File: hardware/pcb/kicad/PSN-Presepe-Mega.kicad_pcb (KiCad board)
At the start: 2 copper layers, 280 x 170 mm, 83 parts, among them J1 12V_IN, K1 G5Q-1_DC12, K10 G5Q-1_DC12, K11 G5Q-1_DC12, K12 G5Q-1_DC12, K13 G5Q-1_DC12, K14 G5Q-1_DC12, K15 G5Q-1_DC12, K16 G5Q-1_DC12, K2 G5Q-1_DC12, K3 G5Q-1_DC12, K4 G5Q-1_DC12, K5 G5Q-1_DC12, K6 G5Q-1_DC12, K7 G5Q-1_DC12, K8 G5Q-1_DC12, K9 G5Q-1_DC12, Q1 IRLZ44N_CIELO_R, Q2 IRLZ44N_CIELO_G, Q3 IRLZ44N_CIELO_B, Q4 IRLZ44N_TRAM_R, Q5 IRLZ44N_TRAM_G, Q6 IRLZ44N_TRAM_B, Q7 IRLZ44N_ALBA_R, Q8 IRLZ44N_ALBA_G, Q9 IRLZ44N_ALBA_B, U1 ULN2803C, U2 ULN2803C

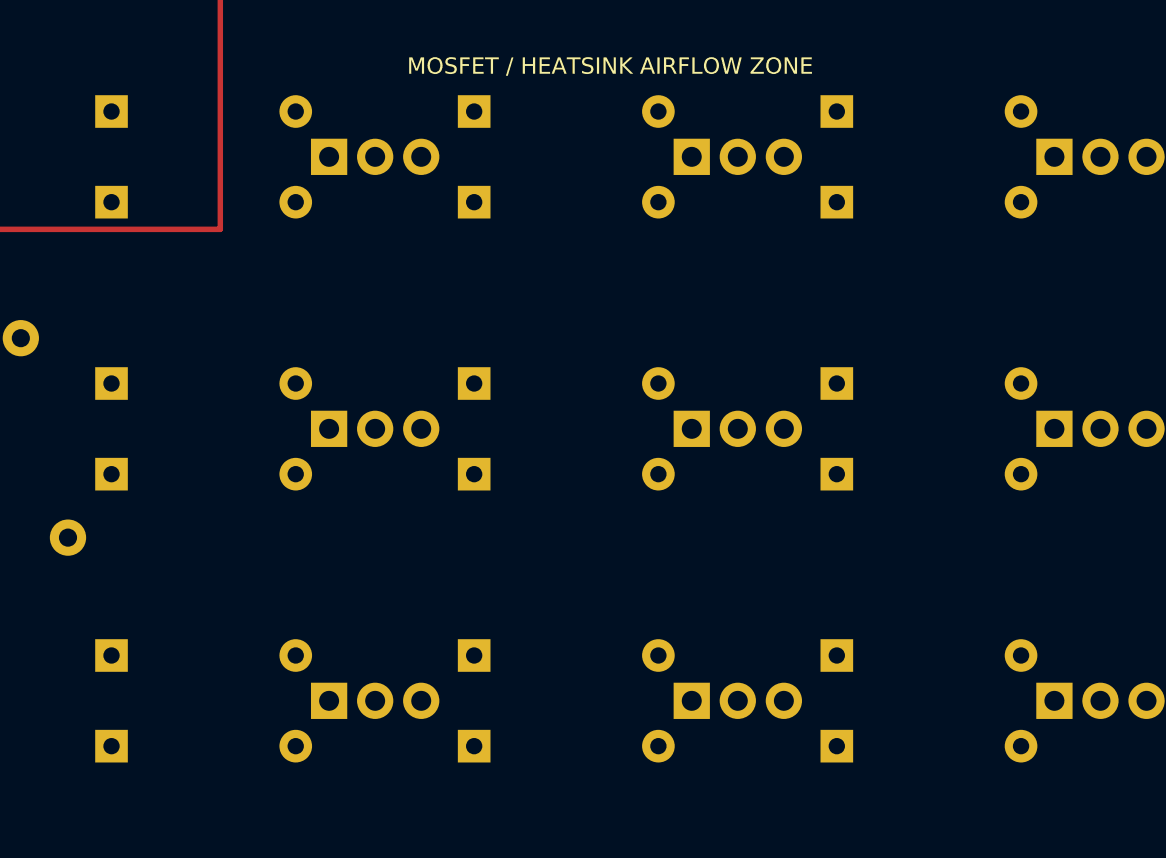
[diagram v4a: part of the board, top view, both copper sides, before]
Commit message: Promote DRC-clean local MOSFET gate routing
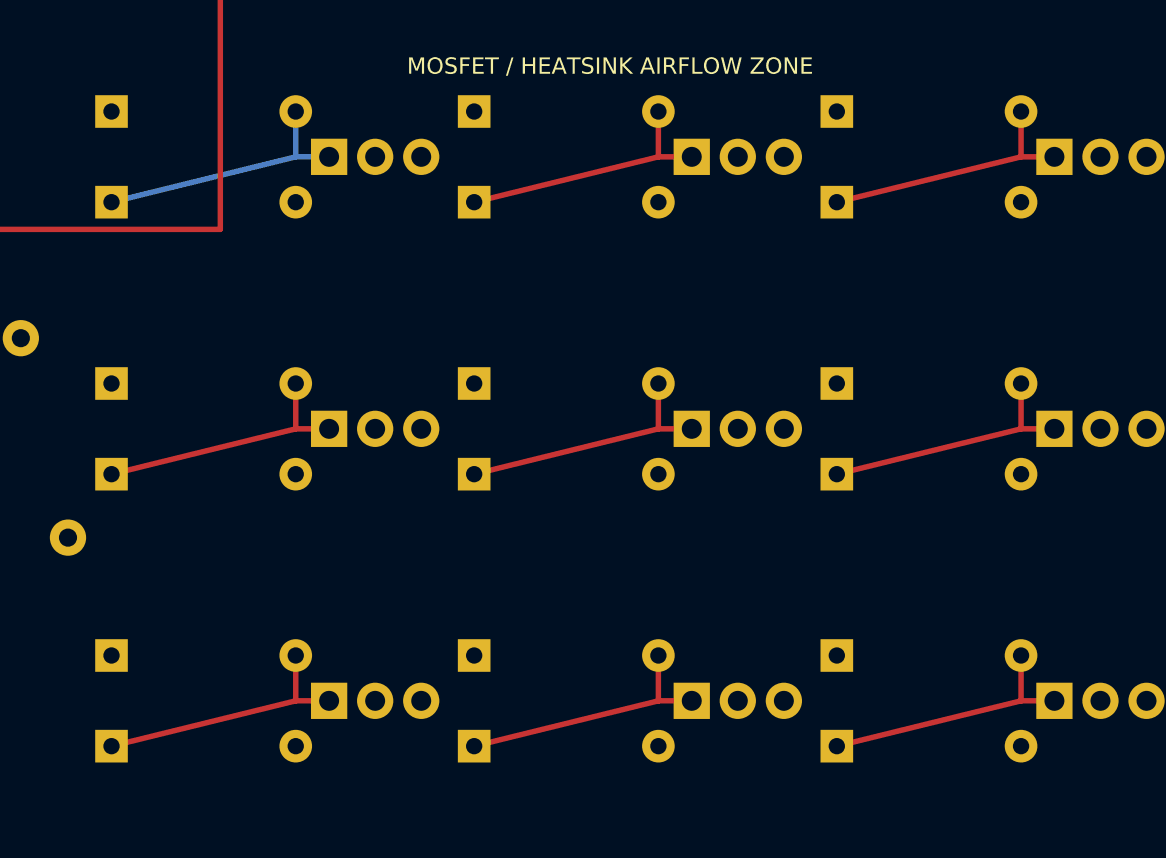
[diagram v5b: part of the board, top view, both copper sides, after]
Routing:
- net GATE_Q9: track 0.00 -> 14.8 mm
- net GATE_Q8: track 0.00 -> 14.8 mm
- net GATE_Q7: track 0.00 -> 14.8 mm
- net GATE_Q6: track 0.00 -> 14.8 mm
- net GATE_Q5: track 0.00 -> 14.8 mm
- net GATE_Q4: track 0.00 -> 14.8 mm
- net GATE_Q3: track 0.00 -> 14.8 mm
- net GATE_Q2: track 0.00 -> 14.8 mm
- net GATE_Q1: track 0.00 -> 14.8 mm
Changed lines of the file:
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@@
   (segment (start 64 139) (end 50.5 139) (width 0.3) (layer "F.Cu") (net 19))
   (segment (start 50.5 139) (end 50.5 145) (width 0.3) (layer "F.Cu") (net 19))
+  (segment (start 68.16 132.5) (end 68.16 135) (width 0.3) (layer "B.Cu") (net 63))
+  (segment (start 68.16 135) (end 70 135) (width 0.3) (layer "B.Cu") (net 63))
+  (segment (start 58 137.5) (end 68.16 135) (width 0.3) (layer "B.Cu") (net 63))
+  (segment (start 88.16 132.5) (end 88.16 135) (width 0.3) (layer "F.Cu") (net 64))
+  (segment (start 88.16 135) (end 90 135) (width 0.3) (layer "F.Cu") (net 64))
+  (segment (start 78 137.5) (end 88.16 135) (width 0.3) (layer "F.Cu") (net 64))
+  (segment (start 108.16 132.5) (end 108.16 135) (width 0.3) (layer "F.Cu") (net 65))
+  (segment (start 108.16 135) (end 110 135) (width 0.3) (layer "F.Cu") (net 65))
+  (segment (start 98 137.5) (end 108.16 135) (width 0.3) (layer "F.Cu") (net 65))
+  (segment (start 68.16 147.5) (end 68.16 150) (width 0.3) (layer "F.Cu") (net 66))
+  (segment (start 68.16 150) (end 70 150) (width 0.3) (layer "F.Cu") (net 66))
+  (segment (start 58 152.5) (end 68.16 150) (width 0.3) (layer "F.Cu") (net 66))
+  (segment (start 88.16 147.5) (end 88.16 150) (width 0.3) (layer "F.Cu") (net 67))
+  (segment (start 88.16 150) (end 90 150) (width 0.3) (layer "F.Cu") (net 67))
+  (segment (start 78 152.5) (end 88.16 150) (width 0.3) (layer "F.Cu") (net 67))
+  (segment (start 108.16 147.5) (end 108.16 150) (width 0.3) (layer "F.Cu") (net 68))
+  (segment (start 108.16 150) (end 110 150) (width 0.3) (layer "F.Cu") (net 68))
+  (segment (start 98 152.5) (end 108.16 150) (width 0.3) (layer "F.Cu") (net 68))
+  (segment (start 68.16 162.5) (end 68.16 165) (width 0.3) (layer "F.Cu") (net 69))
+  (segment (start 68.16 165) (end 70 165) (width 0.3) (layer "F.Cu") (net 69))
+  (segment (start 58 167.5) (end 68.16 165) (width 0.3) (layer "F.Cu") (net 69))
+  (segment (start 88.16 162.5) (end 88.16 165) (width 0.3) (layer "F.Cu") (net 70))
+  (segment (start 88.16 165) (end 90 165) (width 0.3) (layer "F.Cu") (net 70))
+  (segment (start 78 167.5) (end 88.16 165) (width 0.3) (layer "F.Cu") (net 70))
+  (segment (start 108.16 162.5) (end 108.16 165) (width 0.3) (layer "F.Cu") (net 71))
+  (segment (start 108.16 165) (end 110 165) (width 0.3) (layer "F.Cu") (net 71))
+  (segment (start 98 167.5) (end 108.16 165) (width 0.3) (layer "F.Cu") (net 71))
   (gr_rect (start 20 20) (end 300 190) (stroke (width 0.5) (type default)) (fill none) (layer "Edge.Cuts"))
   (gr_rect (start 53 128) (end 118 172) (stroke (width 0.3) (type dash)) (fill none) (layer "Dwgs.User"))

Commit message: Promote DRC-clean relay-1 coil route
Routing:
- net RELAY1_COIL_LOW: track 0.00 -> 17.3 mm
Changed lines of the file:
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@@
   (segment (start 108.16 165) (end 110 165) (width 0.3) (layer "F.Cu") (net 71))
   (segment (start 98 167.5) (end 108.16 165) (width 0.3) (layer "F.Cu") (net 71))
+  (segment (start 145.16 62) (end 147 64) (width 0.3) (layer "F.Cu") (net 36))
+  (segment (start 147 64) (end 157.62 64) (width 0.3) (layer "F.Cu") (net 36))
+  (segment (start 157.62 64) (end 157.62 60) (width 0.3) (layer "F.Cu") (net 36))
   (gr_rect (start 20 20) (end 300 190) (stroke (width 0.5) (type default)) (fill none) (layer "Edge.Cuts"))
   (gr_rect (start 53 128) (end 118 172) (stroke (width 0.3) (type dash)) (fill none) (layer "Dwgs.User"))

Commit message: Promote KiCad-validated K2 coil route
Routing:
- net RELAY2_COIL_LOW: track 0.00 -> 36.1 mm
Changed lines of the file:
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@@
   (segment (start 147 64) (end 157.62 64) (width 0.3) (layer "F.Cu") (net 36))
   (segment (start 157.62 64) (end 157.62 60) (width 0.3) (layer "F.Cu") (net 36))
+  (segment (start 145.16 64.54) (end 148 66.5) (width 0.3) (layer "F.Cu") (net 37))
+  (segment (start 148 66.5) (end 173 66.5) (width 0.3) (layer "F.Cu") (net 37))
+  (segment (start 173 66.5) (end 175.62 64) (width 0.3) (layer "F.Cu") (net 37))
+  (segment (start 175.62 64) (end 175.62 60) (width 0.3) (layer "F.Cu") (net 37))
   (gr_rect (start 20 20) (end 300 190) (stroke (width 0.5) (type default)) (fill none) (layer "Edge.Cuts"))
   (gr_rect (start 53 128) (end 118 172) (stroke (width 0.3) (type dash)) (fill none) (layer "Dwgs.User"))

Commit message: Promote KiCad-validated K3 coil route
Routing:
- net RELAY3_COIL_LOW: track 0.00 -> 56.1 mm
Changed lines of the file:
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@@
   (segment (start 173 66.5) (end 175.62 64) (width 0.3) (layer "F.Cu") (net 37))
   (segment (start 175.62 64) (end 175.62 60) (width 0.3) (layer "F.Cu") (net 37))
+  (segment (start 145.16 67.08) (end 148 69) (width 0.3) (layer "F.Cu") (net 38))
+  (segment (start 148 69) (end 191 69) (width 0.3) (layer "F.Cu") (net 38))
+  (segment (start 191 69) (end 193.62 64) (width 0.3) (layer "F.Cu") (net 38))
+  (segment (start 193.62 64) (end 193.62 60) (width 0.3) (layer "F.Cu") (net 38))
   (gr_rect (start 20 20) (end 300 190) (stroke (width 0.5) (type default)) (fill none) (layer "Edge.Cuts"))
   (gr_rect (start 53 128) (end 118 172) (stroke (width 0.3) (type dash)) (fill none) (layer "Dwgs.User"))
